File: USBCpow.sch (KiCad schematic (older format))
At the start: 7 parts, among them CN1 CON_USB-C-6, J1 Conn_01x05, U1 LM1117-3.3

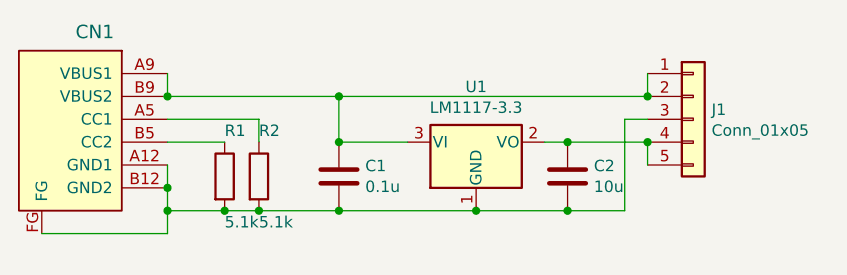
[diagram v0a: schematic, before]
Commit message: 固定用ピンヘッダの穴を追加
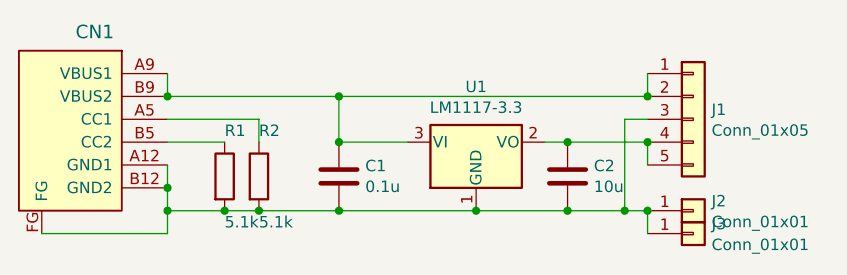
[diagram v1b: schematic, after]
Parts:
- added J2, J3: Conn_01x01, Connector_PinHeader_2.54mm:PinHeader_1x01_P2.54mm_Vertical, symbol Connector_Generic:Conn_01x01
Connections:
- net at C1.2, C2.2, CN1.A12 (GND1)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: now also J2.1 (Pin_1), J3.1 (Pin_1)
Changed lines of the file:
@@
 	5300 2100 5300 2000
 Connection ~ 5300 2000
+$Comp
+L Connector_Generic:Conn_01x01 J2
+U 1 1 5EF68C15
+P 5500 2300
+F 0 "J2" H 5580 2342 50  0000 L CNN
+F 1 "Conn_01x01" H 5580 2251 50  0000 L CNN
+F 2 "Connector_PinHeader_2.54mm:PinHeader_1x01_P2.54mm_Vertical" H 5500 2300 50  0001 C CNN
+F 3 "~" H 5500 2300 50  0001 C CNN
+	1    5500 2300
+	1    0    0    -1
+$EndComp
+$Comp
+L Connector_Generic:Conn_01x01 J3
+U 1 1 5EF6A071
+P 5500 2400
+F 0 "J3" H 5580 2442 50  0000 L CNN
+F 1 "Conn_01x01" H 5580 2351 50  0000 L CNN
+F 2 "Connector_PinHeader_2.54mm:PinHeader_1x01_P2.54mm_Vertical" H 5500 2400 50  0001 C CNN
+F 3 "~" H 5500 2400 50  0001 C CNN
+	1    5500 2400
+	1    0    0    -1
+$EndComp
+Wire Wire Line
+	5200 2300 5300 2300
+Connection ~ 5200 2300
+Wire Wire Line
+	5300 2300 5300 2400
+Connection ~ 5300 2300
 $EndSCHEMATC
